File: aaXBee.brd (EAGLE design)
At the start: 99.1 x 61 mm, 82 parts, among them Q1 IRLML6244TR, SW1 SW1, SW2 RESET, U1 MCP1640D, U2 MCP1640D, U4 ATmega328P-AU, U5 MCP9808, U6 DS3231, Y1 8MHz

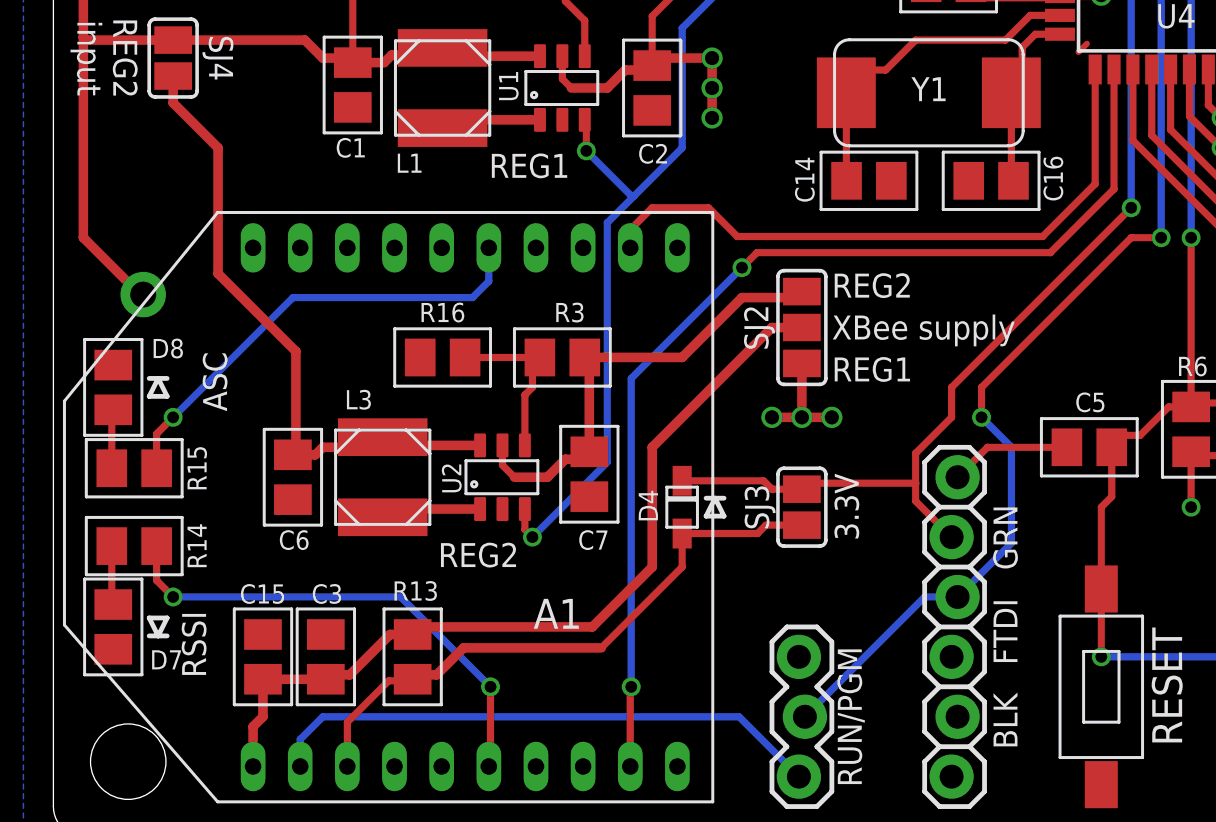
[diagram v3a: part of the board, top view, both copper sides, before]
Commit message: Rename some components to be sequential. Cosmetic adjustments to schematic.
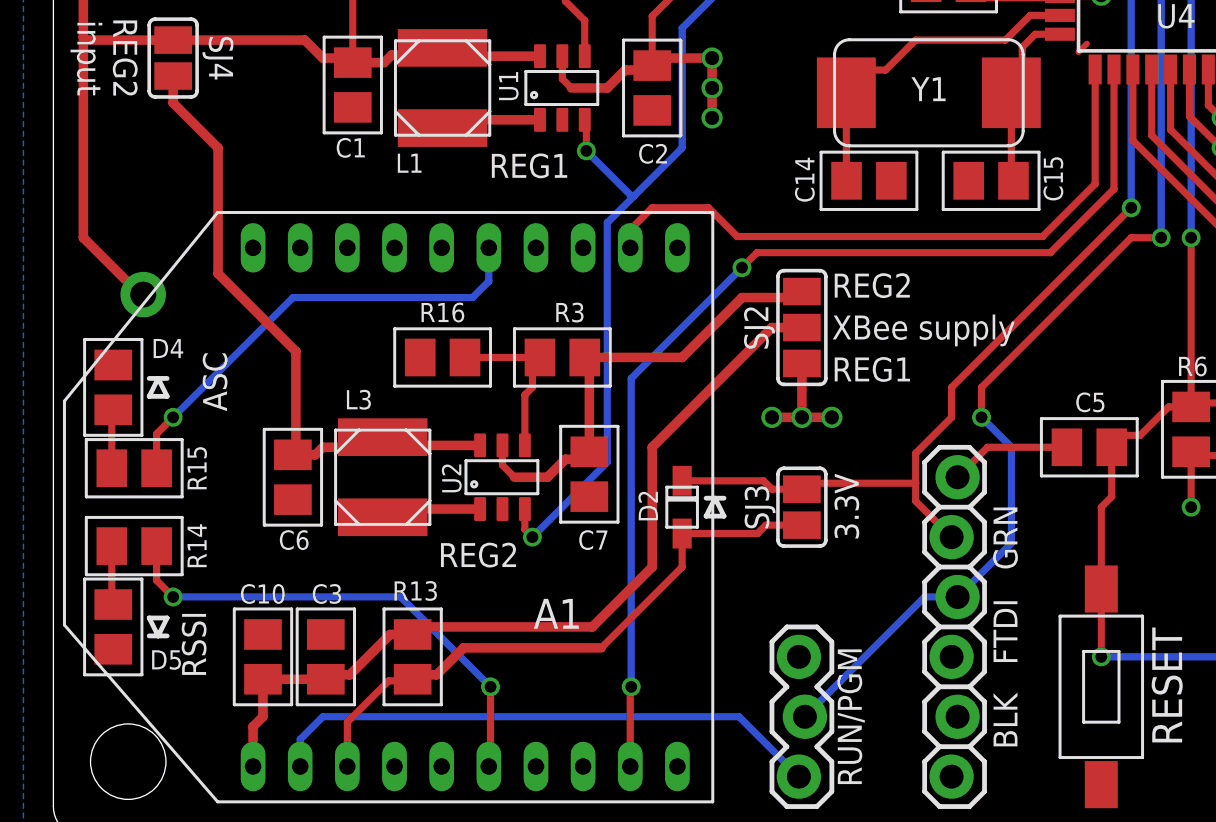
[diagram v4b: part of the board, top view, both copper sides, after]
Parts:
- removed C16: 27pF, _jc:M0805
- removed D8: Green, _jc:D0805
- added C10: 100nF, _jc:M0805
- added D2: 1N4148, _jc:SOD-323F
- C15: value 100nF -> 27pF
- D4: value 1N4148 -> Green; device _jc:SOD-323F -> _jc:D0805
- moved C15 36.9 mm to (39.8, 27.8), turned to 180 degrees
- moved D4 24.7 mm to (2.54, 19.1)
- renumbered D7 to D5
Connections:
- net GND: now also C10.2, D4.K; no longer C16.2, D8.K
- net N$37: now also D2.A; no longer D4.A
- net N$42: now also D4.A; no longer D8.A
- net N$44: now also C15.1; no longer C16.1
- net TXD: now also D2.K; no longer D4.K
- net XBEE_SUPPLY: now also C10.1; no longer C15.1
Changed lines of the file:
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@@
 <element name="LOGO1" library="ohw-logo" package="OSHW_8X150_NOTEXT" value="OSHW_LOGO_8MILX0150-NT" x="34.671" y="41.402"/>
 <element name="LOGO2" library="ohw-logo" package="OSHW_8X150_NOTEXT" value="OSHW_LOGO_8MILX0150-NT" x="95.25" y="68.58"/>
-<element name="C15" library="_jc" package="M0805" value="100nF" x="8.89" y="7.62" smashed="yes" rot="R90">
+<element name="C10" library="_jc" package="M0805" value="100nF" x="8.89" y="7.62" smashed="yes" rot="R90">
 <attribute name="NAME" x="7.898" y="9.882" size="0.8128" layer="25" ratio="16"/>
 <attribute name="VALUE" x="11.39" y="6.12" size="0.8128" layer="27" ratio="16" rot="R90"/>
@@
 <attribute name="VALUE" x="12.74" y="9.12" size="0.8128" layer="27" ratio="16" rot="R270"/>
 </element>
-<element name="D4" library="_jc" package="SOD-323F" value="1N4148" x="26.67" y="13.97" smashed="yes" rot="R90">
+<element name="D2" library="_jc" package="SOD-323F" value="1N4148" x="26.67" y="13.97" smashed="yes" rot="R90">
 <attribute name="NAME" x="25.643" y="13.313" size="0.8128" layer="25" font="vector" ratio="16" rot="R90"/>
 <attribute name="VALUE" x="28.37" y="11.87" size="0.8128" layer="27" font="vector" ratio="16" rot="R90"/>
@@
 <attribute name="VALUE" x="1.929" y="13.121" size="0.8128" layer="27" ratio="16"/>
 </element>
-<element name="D8" library="_jc" package="D0805" value="Green" x="2.54" y="19.05" smashed="yes" rot="R90">
+<element name="D4" library="_jc" package="D0805" value="Green" x="2.54" y="19.05" smashed="yes" rot="R90">
 <attribute name="NAME" x="5.564" y="21.106" size="0.8128" layer="25" ratio="16" rot="R180"/>
 <attribute name="VALUE" x="5.04" y="17.55" size="0.8128" layer="27" ratio="16" rot="R90"/>
 </element>
-<element name="D7" library="_jc" package="D0805A" value="Red" x="2.54" y="8.89" smashed="yes" rot="R270">
+<element name="D5" library="_jc" package="D0805A" value="Red" x="2.54" y="8.89" smashed="yes" rot="R270">
 <attribute name="NAME" x="4.088" y="7.088" size="0.8128" layer="25" ratio="16"/>
 <attribute name="VALUE" x="0.04" y="10.39" size="0.8128" layer="27" ratio="16" rot="R270"/>
@@
 <attribute name="VALUE" x="33.0948" y="25.313" size="0.8128" layer="27" ratio="16"/>
 </element>
-<element name="C16" library="_jc" package="M0805" value="27pF" x="39.7764" y="27.813" smashed="yes" rot="R180">
+<element name="C15" library="_jc" package="M0805" value="27pF" x="39.7764" y="27.813" smashed="yes" rot="R180">
 <attribute name="NAME" x="42.823" y="26.9226" size="0.8128" layer="25" ratio="16" rot="R90"/>
 <attribute name="VALUE" x="41.2764" y="30.313" size="0.8128" layer="27" ratio="16" rot="R180"/>
@@
 <contactref element="PR13" pad="1"/>
 <contactref element="A1" pad="10"/>
-<contactref element="D7" pad="K"/>
-<contactref element="D8" pad="K"/>
-<contactref element="C15" pad="2"/>
+<contactref element="D5" pad="K"/>
+<contactref element="D4" pad="K"/>
+<contactref element="C10" pad="2"/>
 <contactref element="SW2" pad="P$2"/>
 <contactref element="JP6" pad="6"/>
@@
 <contactref element="U4" pad="21"/>
 <contactref element="C14" pad="2"/>
-<contactref element="C16" pad="2"/>
+<contactref element="C15" pad="2"/>
 <contactref element="U4" pad="3"/>
 <contactref element="U4" pad="5"/>
@@
 <signal name="TXD">
 <contactref element="JP2" pad="5"/>
-<contactref element="D4" pad="K"/>
+<contactref element="D2" pad="K"/>
 <contactref element="U4" pad="31"/>
 <contactref element="SJ3" pad="2"/>
@@
 </signal>
 <signal name="N$37">
-<contactref element="D4" pad="A"/>
+<contactref element="D2" pad="A"/>
 <contactref element="A1" pad="3"/>
 <contactref element="R13" pad="2"/>
@@
 <signal name="N$41">
 <contactref element="R14" pad="1"/>
-<contactref element="D7" pad="A"/>
+<contactref element="D5" pad="A"/>
 <wire x1="2.54" y1="9.84" x2="2.479" y2="9.901" width="0.3048" layer="1"/>
 <wire x1="2.479" y1="9.901" x2="2.479" y2="12.319" width="0.3048" layer="1"/>
@@
 <signal name="N$42">
 <contactref element="R15" pad="1"/>
-<contactref element="D8" pad="A"/>
+<contactref element="D4" pad="A"/>
 <wire x1="2.54" y1="18.1" x2="2.479" y2="18.039" width="0.3048" layer="1"/>
 <wire x1="2.479" y1="18.039" x2="2.479" y2="15.621" width="0.3048" layer="1"/>
@@
 <signal name="N$44">
 <contactref element="U4" pad="8"/>
-<contactref element="C16" pad="1"/>
+<contactref element="C15" pad="1"/>
 <contactref element="Y1" pad="P$1"/>
 <wire x1="40.6348" y1="31.5468" x2="40.6348" y2="27.9046" width="0.3048" layer="1"/>
@@
 <contactref element="SJ2" pad="2"/>
 <contactref element="C3" pad="1"/>
-<contactref element="C15" pad="1"/>
+<contactref element="C10" pad="1"/>
 <contactref element="R13" pad="1"/>
 <wire x1="11.557" y1="6.67" x2="8.89" y2="6.67" width="0.4064" layer="1"/>

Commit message: As sent to fab.
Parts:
- removed D5: Red, _jc:D0805A
- removed JP5: Run/Pgm, SparkFun:1X03_LOCK
- removed R17: 249K, _jc:M0805
- removed SW2: RESET, _jc:SWITCH-TACT-6X3.5-SMT
- removed U6: DS3231, _jc:SO-16DW
- added D8: Yellow, _jc:D0805A
- added JP4: GNDSEL, SparkFun:1X03_LOCK
- added R8: 10K, _jc:M0805
- added SW7: SW7, _jc:SWITCH-TACT-6X3.5-SMT
- added U3: MCP9808, _jc:MSOP8
- B1: value CR2016 -> 2xAA; device _jc:BAT-HLD-002-SMT -> _jc:KEYSTONE-2462-NO-HOLES
- B2: value 2xAA -> CR2016; device _jc:KEYSTONE-2462-NO-HOLES -> _jc:BAT-HLD-002-SMT
- C1, C2, C3, C6, C7: value 10uF -> 100nF
- C10, C11, C8, C9: value 100nF -> 10uF
- C14: value 27pF -> 10uF
- C15: value 27pF -> 100nF
- C4, C5: value 100nF -> 27pF
- D1: value Yellow -> 1N4148; device _jc:D0805A -> _jc:SOD-323F-A
- D2: device _jc:SOD-323F -> _jc:SOD-323F-A
- D3: value 1N4148 -> Red; device _jc:SOD-323F -> _jc:D0805A
- JP3: value GNDSEL -> Run/Pgm
- L1: value 4.7uH -> 10uH; device _jc:NRS4018 -> _jc:M0805
- L2: value 10uH -> 4.7uH; device _jc:M0805 -> _jc:NRS4018
- PR13: value (none) -> GND
- R1, R3: value 976K -> 10K
- R10: value 2.2K -> 309K
- R11: value 220 -> 249K
- R12: value 10K -> 976K
- R13: value 4.7K -> 562K
- R14: value 1K -> 4.7K
- R16: value 562K -> 1K
- R2: value 309K -> 47.5K
- R4: value 47.5K -> 2.2K
- R5: value 10K -> 2.2K
- R6: value 10K -> 1K
- R7: value 1K -> 220
- R9: value 2.2K -> 976K
- SJ2: value XBee VR Sel -> Reg2 IP; device jumper:SJ_2 -> jumper:SJ
- SJ3: value /5V -> XBee VR Sel; device jumper:SJ -> jumper:SJ_2
- SJ4: value 5V -> 3.3V
- SW1: value SW1 -> RESET
- U1: value MCP1640D -> ATmega328P-AU; device _jc:SOT23-6 -> atmel:TQFP32-08
- U2: value MCP1640D -> DS3231; device _jc:SOT23-6 -> _jc:SO-16DW
- U4: value ATmega328P-AU -> MCP1640D; device atmel:TQFP32-08 -> _jc:SOT23-6
- U5: value MCP9808 -> MCP1640D; device _jc:MSOP8 -> _jc:SOT23-6
- moved U5 58.5 mm to (19.1, 15.2)
- moved R4 57.8 mm to (67.4, 56.3), turned to 270 degrees
- moved R12 55.7 mm to (22.9, 20.3), turned to 180 degrees
- moved C3 55.4 mm to (58.0, 37.7)
- moved JP3 52.1 mm to (31.8, 2.54), turned to 90 degrees
- moved C11 50.3 mm to (22.7, 15.4)
- moved D3 49.0 mm to (3.25, 8.94)
- moved R10 48.2 mm to (20.7, 36.8), turned to 180 degrees
- moved R9 46.3 mm to (25.4, 36.8), turned to 180 degrees
- moved U2 45.4 mm to (44.7, 52.7), turned to 180 degrees
- moved R11 42.2 mm to (16.9, 37.6), turned to 90 degrees
- moved C9 40.1 mm to (25.4, 31.8)
- moved L1 39.0 mm to (55.5, 33.1), turned to 90 degrees
- moved L2 39.0 mm to (16.5, 31.8), turned to 270 degrees
- moved C7 37.1 mm to (57.9, 27.2)
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- renumbered JP6 to JP1
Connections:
- removed net 32KHZ: U6.1
- net /RESET: now also C6.1, D1.A, R1.1, SW1.P$1, U1.29; no longer C5.1, D3.A, R6.1, SW2.P$1, U4.29
- net /SS: now also U1.14; no longer U4.14
- net ADC0: now also U1.23; no longer U4.23
- net ADC1: now also U1.24; no longer U4.24
- net ADC2: now also U1.25; no longer U4.25
- net ADC3: now also U1.26; no longer U4.26
- net ADC6: now also C7.2, R3.2, U1.19; no longer C4.2, R5.2, U4.19
- net ADC7: now also C7.1, R2.2, R3.1, U1.22; no longer C4.1, R4.2, R5.1, U4.22
- net AREF: now also C3.1, U1.20; no longer C13.1, U4.20
- net ASC: now also R16.2; no longer R15.2
- net BAT: now also B1.POS, C8.1, L2.P$1, R2.1, SJ2.1, U4.6; no longer B2.POS, C1.1, L1.P$1, R4.1, SJ4.1, U1.6
- net CTS: now also U1.9; no longer U4.9
- net EN: now also U1.2, U4.3, U5.3; no longer U1.3, U2.3, U4.2
- net GND: now also C4.2, C5.2, D3.K, D8.K, JP4.3, R11.2, R13.2, R8.2, SW7.P$2, U1.21, U1.3, U1.5, U2.10, U2.11, U2.12, U2.13, U2.5, U2.6, U2.7, U2.8, U2.9, U3.4, U3.5, U3.6, U3.7, U4.2, U5.2; no longer C6.2, C7.2, D1.K, D5.K, JP3.3, R12.2, R16.2, R17.2, SW2.P$2, U1.2, U2.2, U4.21, U4.3, U4.5, U5.4, U5.5, U5.6, U5.7, U6.10, U6.11, U6.12, U6.13, U6.5, U6.6, U6.7, U6.8, U6.9
- net INT: now also U1.1, U2.3; no longer U4.1, U6.3
- net MISO: now also U1.16; no longer U4.16
- net MOSI: now also U1.15; no longer U4.15
- net N$1: now also B2.POS1, U2.14; no longer B1.POS1, U6.14
- net N$12: now also R12.2, R13.1, U5.4; no longer R16.1, R3.2, U2.4
- net N$13: now also U5.1; no longer U2.1
- net N$2: now also D8.A, R6.1; no longer D1.A, R7.1
- net N$24: now also R7.1, R8.1; no longer R11.1, R12.1
- net N$35: now also C10.1, SJ2.2, U5.6; no longer C6.1, SJ4.2, U2.6
- net N$36: now also JP4.1; no longer JP3.1
- net N$37: now also R14.2, SJ4.1; no longer R13.2, SJ3.1
- net N$38: now also JP3.1; no longer JP5.1
- net N$39: now also C11.1, R12.1, SJ3.1, U5.5; no longer C7.1, R3.1, SJ2.1, U2.5
- net N$41: now also D3.A, R15.1; no longer D5.A, R14.1
- net N$42: now also R16.1; no longer R15.1
- net N$43: now also C4.1, U1.7; no longer C14.1, U4.7
- net N$44: now also C5.1, U1.8; no longer C15.1, U4.8
- net N$46: now also C2.1, L1.2, U1.18; no longer C12.1, L2.2, U4.18
- net N$6: now also R10.1, R9.2, U4.4; no longer R1.2, R2.1, U1.4
- net N$7: now also L2.P$2, U4.1; no longer L1.P$2, U1.1
- net N$8: now also R10.2, R11.1; no longer R17.1, R2.2
- net PB0: now also R6.2, U1.12; no longer R7.2, U4.12
- net PD7: now also SW7.P$1, U1.11; no longer SW1.P$1, U4.11
- net PPWR: now also C12.1, C13.1, U1.32, U2.2, U3.8; no longer C11.1, C9.1, U4.32, U5.8, U6.2
- net RSSI: now also R15.2; no longer R14.2
- net RST: now also C6.2; no longer C5.2
- net RXD: now also JP3.2, U1.30; no longer JP5.2, U4.30
- net SCK: now also U1.17; no longer U4.17
- net SCL: now also R5.2, U1.28, U2.16, U3.2; no longer R10.2, U4.28, U5.2, U6.16
- net SDA: now also R4.2, U1.27, U2.15, U3.1; no longer R9.2, U4.27, U5.1, U6.15
- net SGND: now also JP4.2; no longer JP3.2
- net SLP: now also U1.10; no longer U4.10
- net SPWR: now also R7.2, U1.13; no longer R11.2, U4.13
- net TXD: now also SJ4.2, U1.31; no longer SJ3.2, U4.31
- net VCC: now also C1.1, C9.1, D1.K, L1.1, R1.2, R4.1, R5.1, SJ3.3, U1.4, U1.6, U4.5; no longer C2.1, C8.1, D3.K, L2.1, R1.1, R10.1, R6.2, SJ2.3, U1.5, U4.4, U4.6
- net XBEE_SUPPLY: now also C14.1, C15.1, R14.1, SJ3.2; no longer C10.1, C3.1, R13.1, SJ2.2
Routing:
- net RST: track 5.16 -> 8.83 mm
- net /RESET: track 70.6 -> 72.0 mm
- net N$39: track 19.6 -> 18.3 mm
- net BAT: track 56.9 -> 55.5 mm
- net VCC: track 84.2 -> 83.0 mm
- net N$35: track 26.8 -> 25.7 mm
- net RSSI: track 20.9 -> 19.9 mm
- net ASC: track 19.6 -> 19.1 mm
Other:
- board text added: "CC BY-SA 0315 jc"
- board text added: "Double-A XBee Sensor Node CC BY-SA 0315 jc v1 http://goo.gl/4g7J1w"
- board text removed: "CC BY-SA 0215 jc"
